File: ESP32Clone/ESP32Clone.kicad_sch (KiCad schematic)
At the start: 41 parts, among them J1 Connector, USB-TYPE-C-16P, J2 Conn_01x08_Pin, J3 Conn_01x08_Pin, U1 TPS54331DR, U2 ESP32-C3FH4, X1 40MHz, 15pF

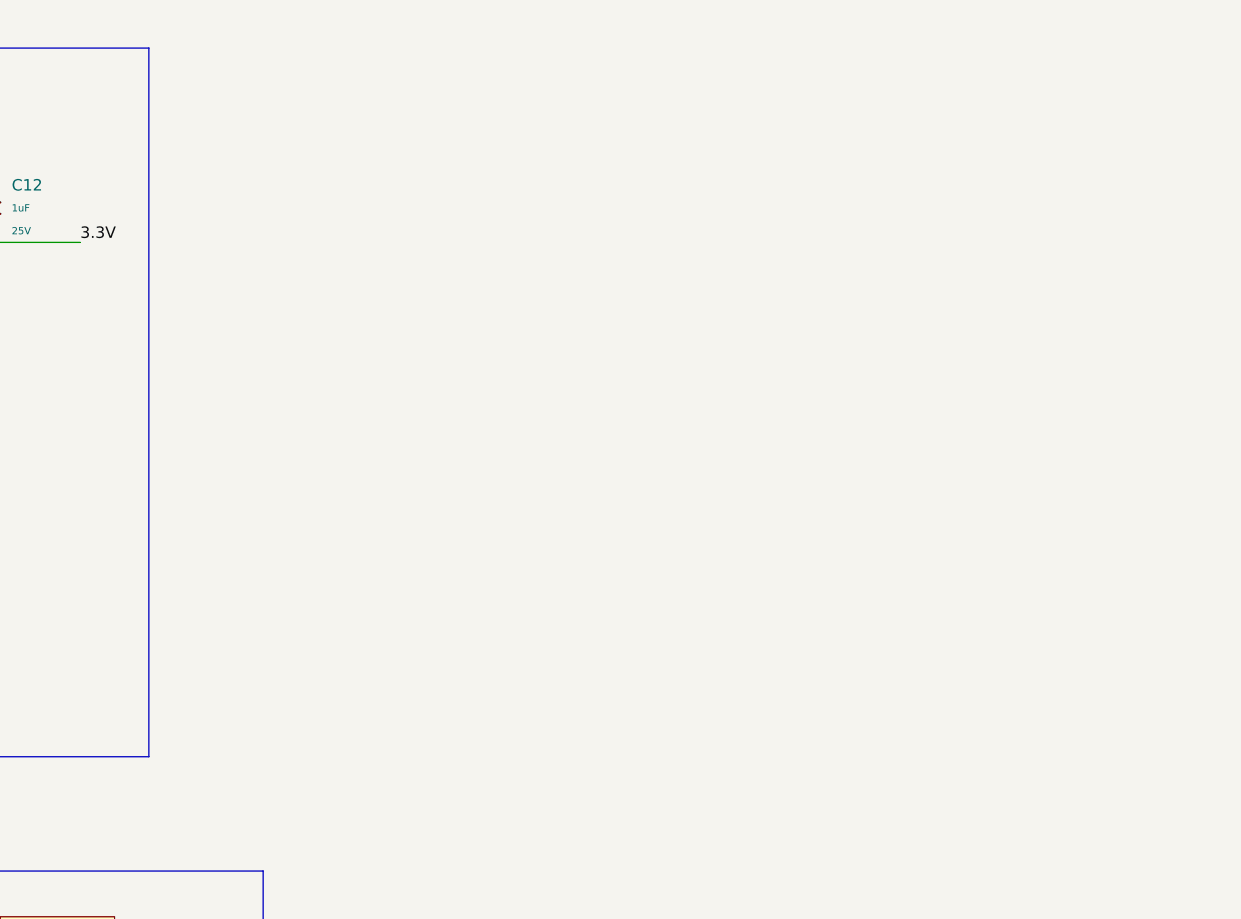
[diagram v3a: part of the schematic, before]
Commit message: Added IC2 devices
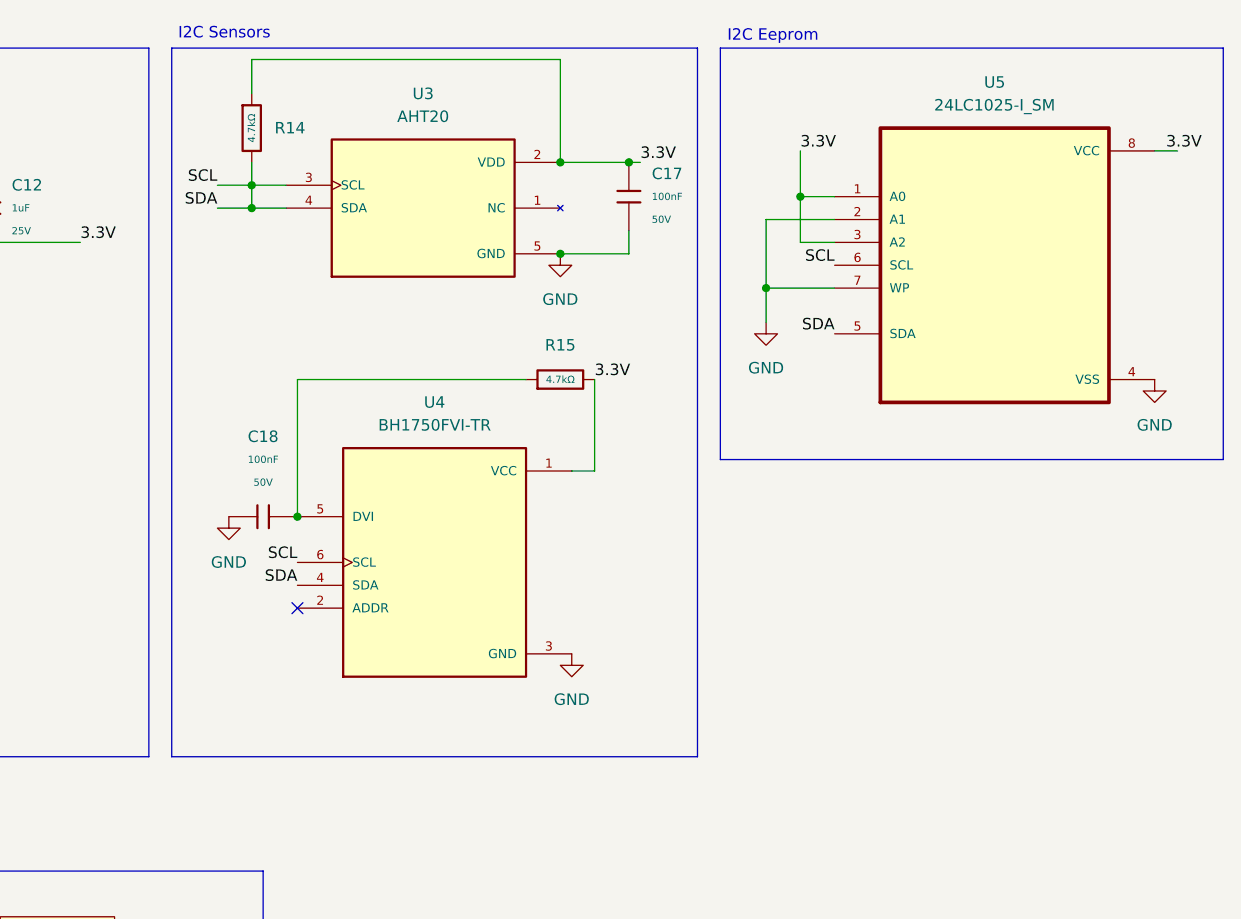
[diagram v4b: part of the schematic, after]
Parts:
- added C17, C18: 100nF, PCM_JLCPCB:C_0603, symbol PCM_JLCPCB-Capacitors:0603,100nF
- added R14, R15: 4.7kΩ, PCM_JLCPCB:R_0805, symbol PCM_JLCPCB-Resistors:0805,4.7kΩ
- added U3: AHT20, AHT20:PSON100P300X300X110-6N, symbol AHT20:AHT20
- added U4: BH1750FVI-TR, BH1750FVI-TR:XDCR_BH1750FVI-TR, symbol BH1750FVI-TR:BH1750FVI-TR
- added U5: 24LC1025-I_SM, 24LC1025-I_SM:SOIC127P794X202-8N, symbol 24LC1025-I_SM:24LC1025-I_SM
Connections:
- net SDA is gone; now on net SCL: J3.4 (Pin_4), R8.1, U2.14 (GPIO8)
- net 3.3V: now also C17.1, R14.1, R15.2, U3.2 (VDD), U4.1 (VCC), U5.1 (A0), U5.3 (A2), U5.8 (VCC)
- net GND: now also C17.2, C18.1, U3.5 (GND), U4.3 (GND), U5.2 (A1), U5.4 (VSS), U5.7 (WP)
- net SCL: now also R14.2, U3.3 (SCL), U3.4 (SDA), U4.4 (SDA), U4.6 (SCL), U5.5 (SDA), U5.6 (SCL)
- new net: C18.2, R15.1, U4.5 (DVI)
- new net: U3.1 (NC), U3.6 (NC)
- no-connect marks 13 -> 14
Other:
- note added: "I2C Eeprom"
- note added: "I2C Sensors"
